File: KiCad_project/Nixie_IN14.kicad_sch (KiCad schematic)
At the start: 62 parts, among them J1 Conn_01x10_Pin, J2 Conn_01x07_Pin, J3 Conn_01x07_Pin, J4 Conn_01x10_Pin, J5 Conn_01x07_Pin, J6 Conn_01x07_Pin, J7 USB_C_Receptacle_PowerOnly_6P, Q1 IRF540N, Q2 MMBTA42, U1 BME280_module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

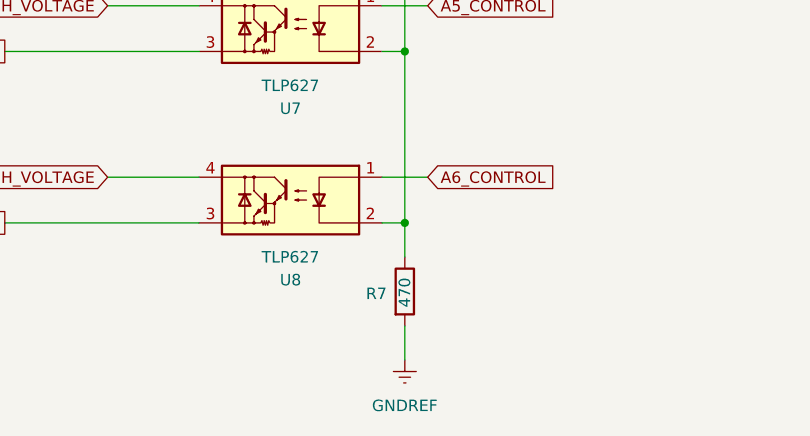
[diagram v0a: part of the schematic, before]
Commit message: update dot night brightness. Updated PCB for previous commit
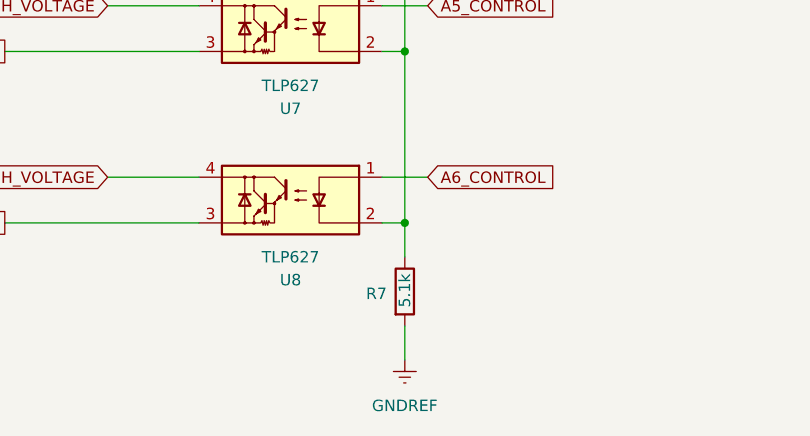
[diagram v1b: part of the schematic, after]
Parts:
- R7: value 470 -> 5.1k
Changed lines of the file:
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@@
 			)
 		)
-		(property "Value" "470"
+		(property "Value" "5.1k"
 			(at 156.21 382.778 90)
 			(effects
